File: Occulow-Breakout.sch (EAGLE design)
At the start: 10 parts

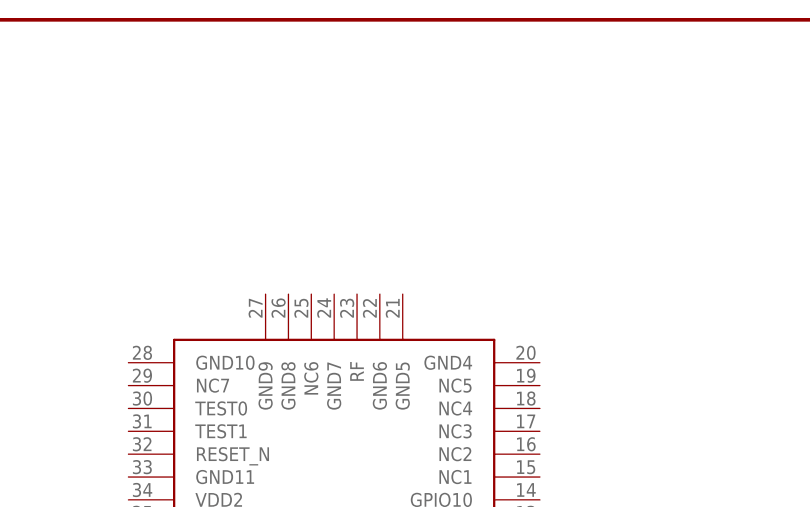
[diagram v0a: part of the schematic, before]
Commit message: Added SMA jack, RF connection for LoRa
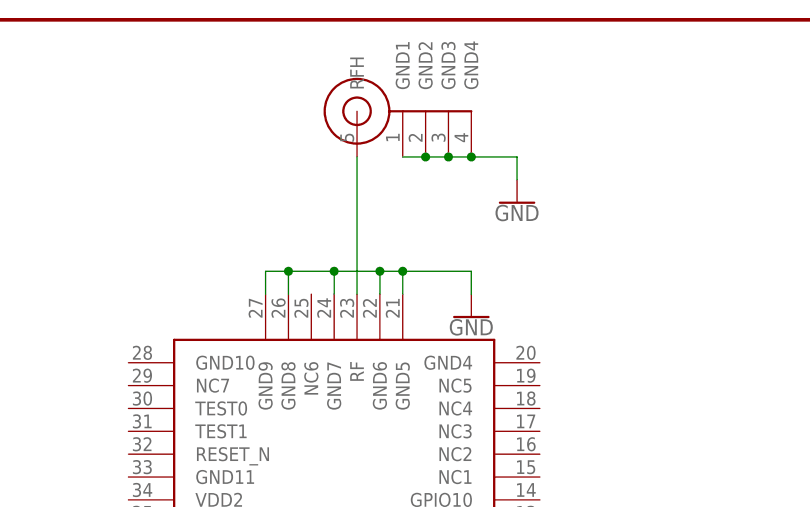
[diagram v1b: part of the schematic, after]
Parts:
- added U$3: SMA-JACKFEMALE, SMA-JACK:SMA-JACKFEMALE
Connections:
- new net N$1: U$1.RF, U$3.RFH
- net GND: now also U$1.GND5, U$1.GND6, U$1.GND7, U$1.GND8, U$1.GND9, U$3.GND1, U$3.GND2, U$3.GND3, U$3.GND4
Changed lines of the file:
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@@
 <part name="GND4" library="SparkFun-PowerSymbols" deviceset="GND" device=""/>
 <part name="SUPPLY2" library="SparkFun-PowerSymbols" deviceset="VCC" device=""/>
+<part name="U$3" library="SMA-JACK" deviceset="SMA-JACK" device="FEMALE"/>
+<part name="GND5" library="SparkFun-PowerSymbols" deviceset="GND" device=""/>
+<part name="GND6" library="SparkFun-PowerSymbols" deviceset="GND" device=""/>
 </parts>
 <sheets>
@@
 <instance part="GND4" gate="1" x="274.32" y="10.16"/>
 <instance part="SUPPLY2" gate="G$1" x="248.92" y="68.58"/>
+<instance part="U$3" gate="G$1" x="327.66" y="170.18"/>
+<instance part="GND5" gate="1" x="345.44" y="160.02"/>
+<instance part="GND6" gate="1" x="340.36" y="147.32"/>
 </instances>
 <busses>
@@
 <wire x1="274.32" y1="27.94" x2="274.32" y2="12.7" width="0.1524" layer="91"/>
 </segment>
+<segment>
+<pinref part="U$3" gate="G$1" pin="GND1"/>
+<pinref part="U$3" gate="G$1" pin="GND2"/>
+<wire x1="332.74" y1="165.1" x2="335.28" y2="165.1" width="0.1524" layer="91"/>
+<pinref part="U$3" gate="G$1" pin="GND3"/>
+<wire x1="335.28" y1="165.1" x2="337.82" y2="165.1" width="0.1524" layer="91"/>
+<junction x="335.28" y="165.1"/>
+<pinref part="U$3" gate="G$1" pin="GND4"/>
+<wire x1="337.82" y1="165.1" x2="340.36" y2="165.1" width="0.1524" layer="91"/>
+<junction x="337.82" y="165.1"/>
+<wire x1="340.36" y1="165.1" x2="345.44" y2="165.1" width="0.1524" layer="91"/>
+<junction x="340.36" y="165.1"/>
+<pinref part="GND5" gate="1" pin="GND"/>
+<wire x1="345.44" y1="165.1" x2="345.44" y2="162.56" width="0.1524" layer="91"/>
+</segment>
+<segment>
+<pinref part="U$1" gate="G$1" pin="GND9"/>
+<wire x1="317.5" y1="149.86" x2="317.5" y2="152.4" width="0.1524" layer="91"/>
+<wire x1="317.5" y1="152.4" x2="320.04" y2="152.4" width="0.1524" layer="91"/>
+<pinref part="U$1" gate="G$1" pin="GND8"/>
+<wire x1="320.04" y1="152.4" x2="325.12" y2="152.4" width="0.1524" layer="91"/>
+<wire x1="325.12" y1="152.4" x2="330.2" y2="152.4" width="0.1524" layer="91"/>
+<wire x1="330.2" y1="152.4" x2="332.74" y2="152.4" width="0.1524" layer="91"/>
+<wire x1="332.74" y1="152.4" x2="340.36" y2="152.4" width="0.1524" layer="91"/>
+<wire x1="320.04" y1="149.86" x2="320.04" y2="152.4" width="0.1524" layer="91"/>
+<junction x="320.04" y="152.4"/>
+<pinref part="U$1" gate="G$1" pin="GND7"/>
+<wire x1="325.12" y1="149.86" x2="325.12" y2="152.4" width="0.1524" layer="91"/>
+<junction x="325.12" y="152.4"/>
+<pinref part="U$1" gate="G$1" pin="GND6"/>
+<wire x1="330.2" y1="149.86" x2="330.2" y2="152.4" width="0.1524" layer="91"/>
+<junction x="330.2" y="152.4"/>
+<pinref part="U$1" gate="G$1" pin="GND5"/>
+<wire x1="332.74" y1="149.86" x2="332.74" y2="152.4" width="0.1524" layer="91"/>
+<junction x="332.74" y="152.4"/>
+<pinref part="GND6" gate="1" pin="GND"/>
+<wire x1="340.36" y1="149.86" x2="340.36" y2="152.4" width="0.1524" layer="91"/>
+</segment>
 </net>
 <net name="N$2" class="0">
@@
 </segment>
 </net>
+<net name="N$1" class="0">
+<segment>
+<pinref part="U$1" gate="G$1" pin="RF"/>
+<pinref part="U$3" gate="G$1" pin="RFH"/>
+<wire x1="327.66" y1="149.86" x2="327.66" y2="165.1" width="0.1524" layer="91"/>
+</segment>
+</net>

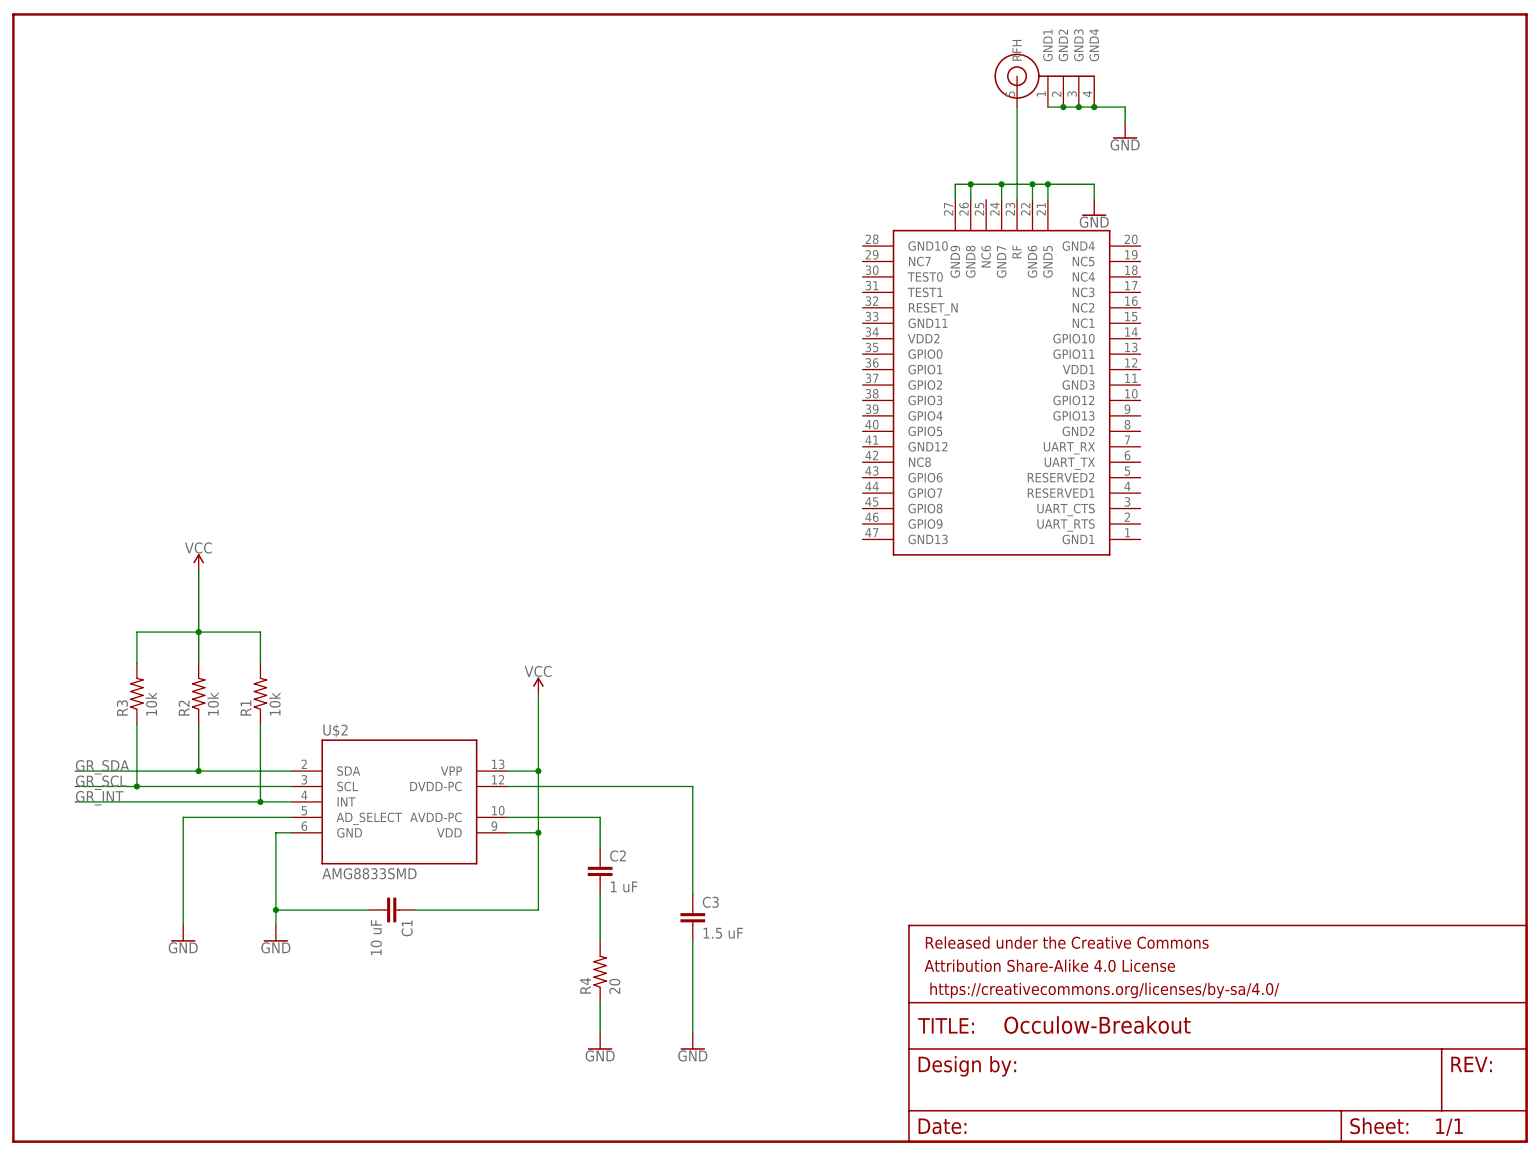
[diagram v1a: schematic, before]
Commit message: Added PIR sensor
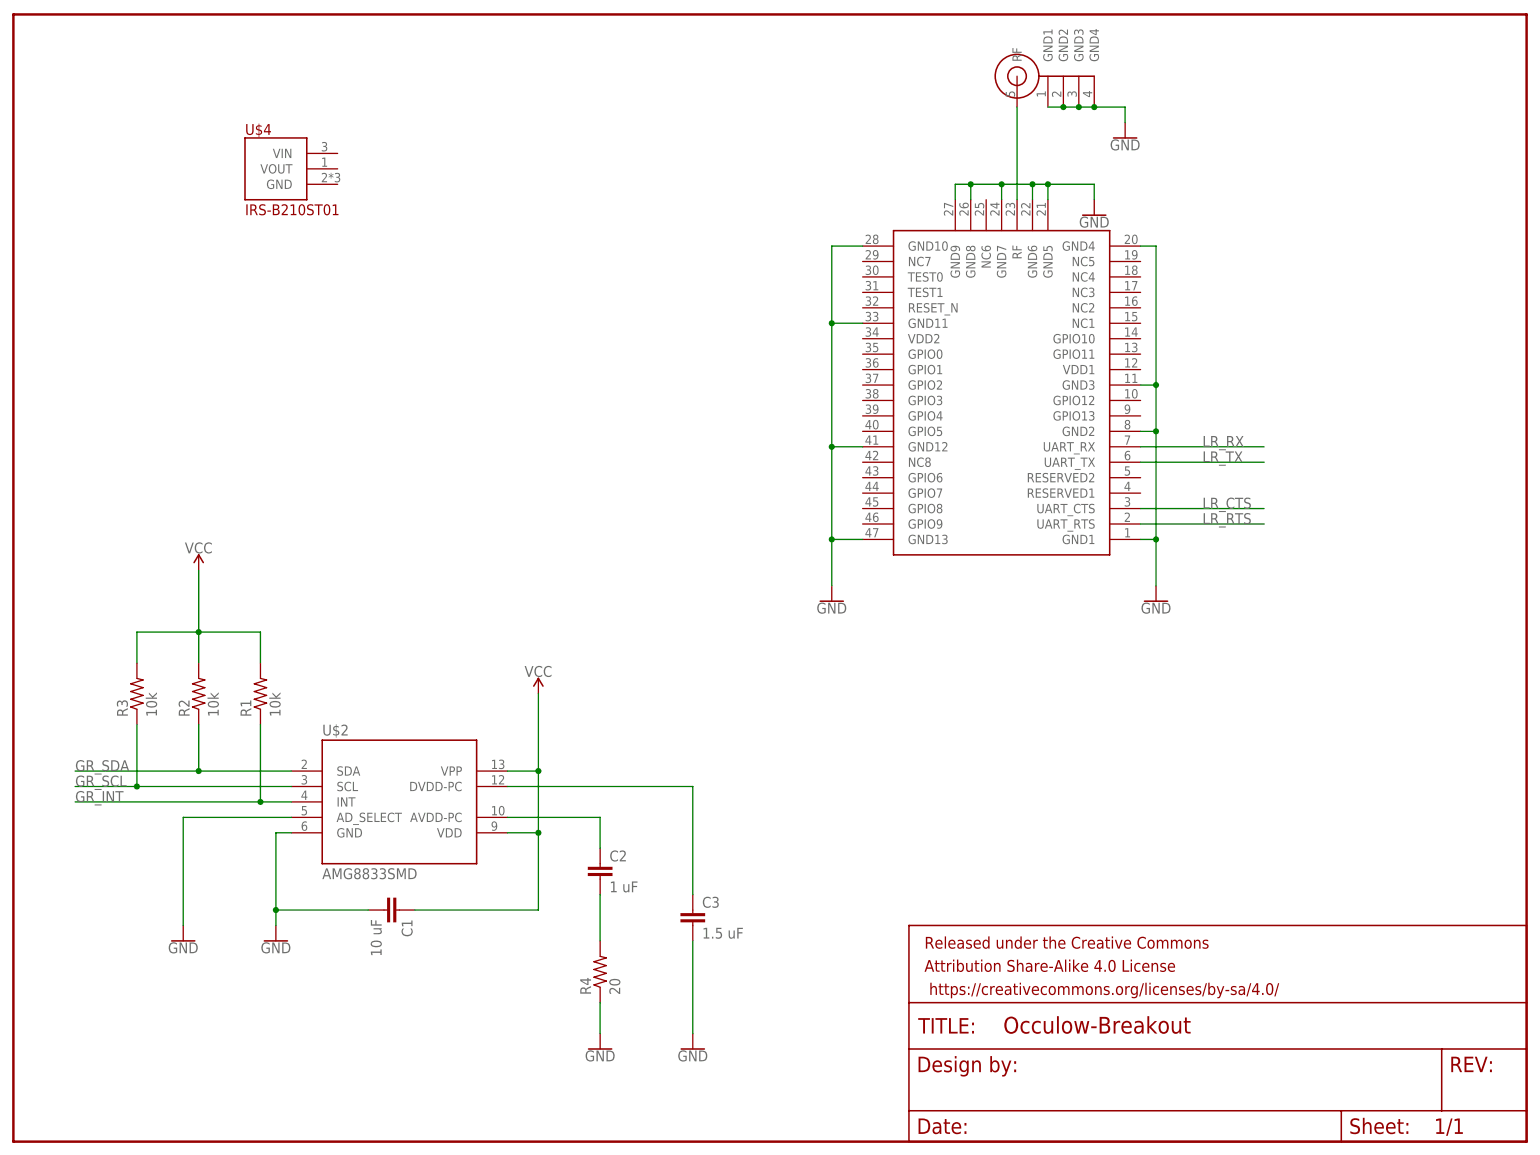
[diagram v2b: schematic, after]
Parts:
- added U$4: IRS-B210ST01, PIR:IRS-B210ST01
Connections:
- new net LR_CTS: U$1.UART_CTS
- new net LR_RTS: U$1.UART_RTS
- new net LR_RX: U$1.UART_RX
- new net LR_TX: U$1.UART_TX
- net GND: now also U$1.GND1, U$1.GND10, U$1.GND11, U$1.GND12, U$1.GND13, U$1.GND2, U$1.GND3, U$1.GND4
- net N$1: now also U$3.RF; no longer U$3.RFH
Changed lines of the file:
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@@
 <part name="GND5" library="SparkFun-PowerSymbols" deviceset="GND" device=""/>
 <part name="GND6" library="SparkFun-PowerSymbols" deviceset="GND" device=""/>
+<part name="GND7" library="SparkFun-PowerSymbols" deviceset="GND" device=""/>
+<part name="GND8" library="SparkFun-PowerSymbols" deviceset="GND" device=""/>
+<part name="U$4" library="PIR" deviceset="IRS-B210ST01" device=""/>
 </parts>
 <sheets>
@@
 <instance part="GND5" gate="1" x="345.44" y="160.02"/>
 <instance part="GND6" gate="1" x="340.36" y="147.32"/>
+<instance part="GND7" gate="1" x="350.52" y="83.82"/>
+<instance part="GND8" gate="1" x="297.18" y="83.82"/>
+<instance part="U$4" gate="G$1" x="205.74" y="154.94"/>
 </instances>
 <busses>
@@
 <wire x1="340.36" y1="149.86" x2="340.36" y2="152.4" width="0.1524" layer="91"/>
 </segment>
+<segment>
+<pinref part="U$1" gate="G$1" pin="GND4"/>
+<pinref part="GND7" gate="1" pin="GND"/>
+<wire x1="347.98" y1="142.24" x2="350.52" y2="142.24" width="0.1524" layer="91"/>
+<wire x1="350.52" y1="142.24" x2="350.52" y2="119.38" width="0.1524" layer="91"/>
+<pinref part="U$1" gate="G$1" pin="GND3"/>
+<wire x1="350.52" y1="119.38" x2="350.52" y2="111.76" width="0.1524" layer="91"/>
+<wire x1="350.52" y1="111.76" x2="350.52" y2="93.98" width="0.1524" layer="91"/>
+<wire x1="350.52" y1="93.98" x2="350.52" y2="86.36" width="0.1524" layer="91"/>
+<wire x1="347.98" y1="119.38" x2="350.52" y2="119.38" width="0.1524" layer="91"/>
+<junction x="350.52" y="119.38"/>
+<pinref part="U$1" gate="G$1" pin="GND2"/>
+<wire x1="347.98" y1="111.76" x2="350.52" y2="111.76" width="0.1524" layer="91"/>
+<junction x="350.52" y="111.76"/>
+<pinref part="U$1" gate="G$1" pin="GND1"/>
+<wire x1="347.98" y1="93.98" x2="350.52" y2="93.98" width="0.1524" layer="91"/>
+<junction x="350.52" y="93.98"/>
+</segment>
+<segment>
+<pinref part="U$1" gate="G$1" pin="GND10"/>
+<pinref part="GND8" gate="1" pin="GND"/>
+<wire x1="302.26" y1="142.24" x2="297.18" y2="142.24" width="0.1524" layer="91"/>
+<wire x1="297.18" y1="142.24" x2="297.18" y2="129.54" width="0.1524" layer="91"/>
+<pinref part="U$1" gate="G$1" pin="GND11"/>
+<wire x1="297.18" y1="129.54" x2="297.18" y2="109.22" width="0.1524" layer="91"/>
+<wire x1="297.18" y1="109.22" x2="297.18" y2="93.98" width="0.1524" layer="91"/>
+<wire x1="297.18" y1="93.98" x2="297.18" y2="86.36" width="0.1524" layer="91"/>
+<wire x1="302.26" y1="129.54" x2="297.18" y2="129.54" width="0.1524" layer="91"/>
+<junction x="297.18" y="129.54"/>
+<pinref part="U$1" gate="G$1" pin="GND12"/>
+<wire x1="302.26" y1="109.22" x2="297.18" y2="109.22" width="0.1524" layer="91"/>
+<junction x="297.18" y="109.22"/>
+<pinref part="U$1" gate="G$1" pin="GND13"/>
+<wire x1="302.26" y1="93.98" x2="297.18" y2="93.98" width="0.1524" layer="91"/>
+<junction x="297.18" y="93.98"/>
+</segment>
 </net>
 <net name="N$2" class="0">
@@
 <segment>
 <pinref part="U$1" gate="G$1" pin="RF"/>
-<pinref part="U$3" gate="G$1" pin="RFH"/>
+<pinref part="U$3" gate="G$1" pin="RF"/>
 <wire x1="327.66" y1="149.86" x2="327.66" y2="165.1" width="0.1524" layer="91"/>
 </segment>
 </net>
+<net name="LR_RX" class="0">
+<segment>
+<pinref part="U$1" gate="G$1" pin="UART_RX"/>
+<wire x1="347.98" y1="109.22" x2="368.3" y2="109.22" width="0.1524" layer="91"/>
+<label x="358.14" y="109.22" size="1.778" layer="95"/>
+</segment>
+</net>
+<net name="LR_TX" class="0">
+<segment>
+<pinref part="U$1" gate="G$1" pin="UART_TX"/>
+<wire x1="347.98" y1="106.68" x2="368.3" y2="106.68" width="0.1524" layer="91"/>
+<label x="358.14" y="106.68" size="1.778" layer="95"/>
+</segment>
+</net>
+<net name="LR_CTS" class="0">
+<segment>
+<pinref part="U$1" gate="G$1" pin="UART_CTS"/>
+<wire x1="347.98" y1="99.06" x2="368.3" y2="99.06" width="0.1524" layer="91"/>
+<label x="358.14" y="99.06" size="1.778" layer="95"/>
+</segment>
+</net>
+<net name="LR_RTS" class="0">
+<segment>
+<pinref part="U$1" gate="G$1" pin="UART_RTS"/>
+<wire x1="347.98" y1="96.52" x2="368.3" y2="96.52" width="0.1524" layer="91"/>
+<label x="358.14" y="96.52" size="1.778" layer="95"/>
+</segment>
+</net>
